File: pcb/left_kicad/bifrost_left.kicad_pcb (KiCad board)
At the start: 2 copper layers, 142.9 x 80.3 mm, 66 parts, among them J1 HRO_TYPE-C-31-M-12, J2 Conn_01x02, J3 Conn_01x06, Q1 AO3401A, Q2 2N7002, Q3 AO3401A, SW1 1.5U, SW10 SW_Push, SW11 SW_Push, SW12 1.25U, SW13 SW_Push, SW14 SW_Push, SW15 SW_Push, SW16 SW_Push, SW17 SW_Push, SW18 SW_Push, SW19 SW_Push, SW2 1.75U, SW20 SW_Push, SW21 SW_Push, SW3 SW_Push, SW4 1.25U, SW5 SW_Push, SW6 SW_Push, SW7 SW_Push, SW8 1.25U, SW9 SW_Push, T1 SW_Push_Shielded, U1 MDBT50Q-1MV2, U2 TP4057, U3 SRV05-4, X1 32.768kHz

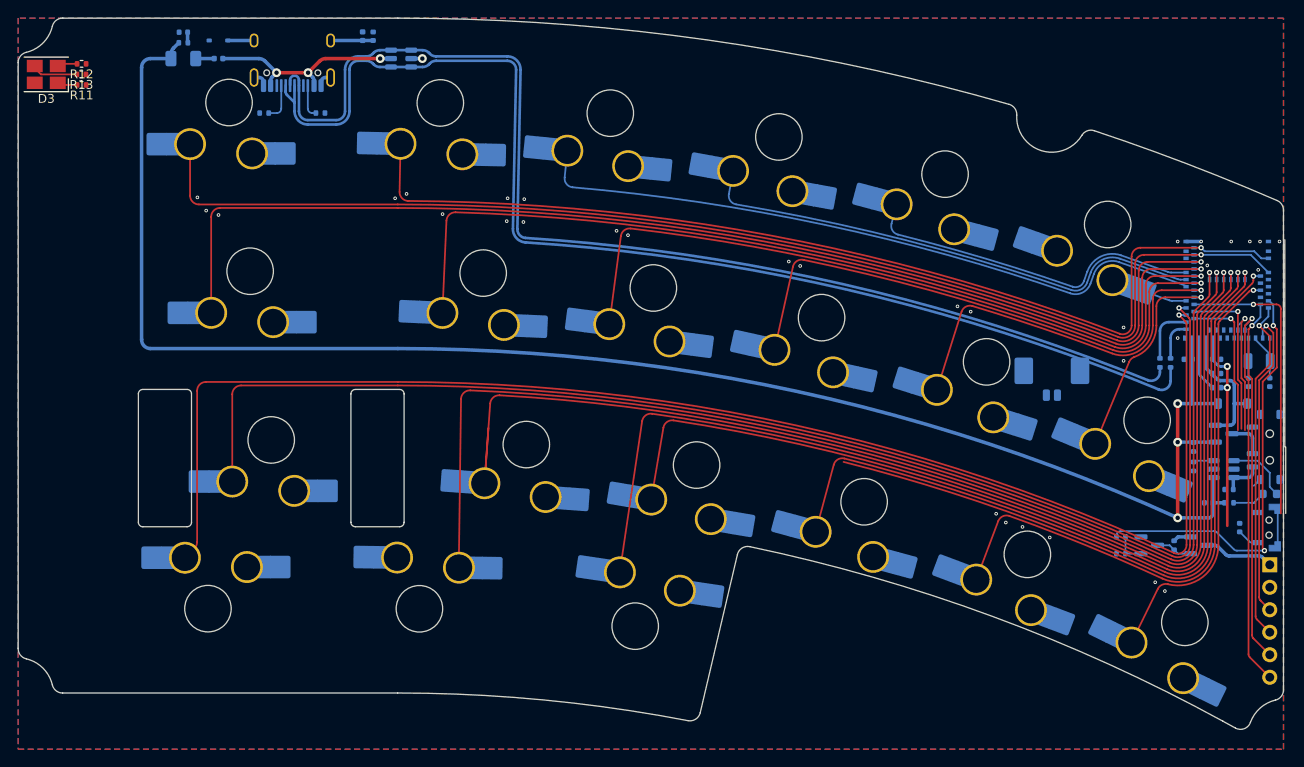
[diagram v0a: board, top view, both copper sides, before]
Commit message: Update KiCad keyboard designs
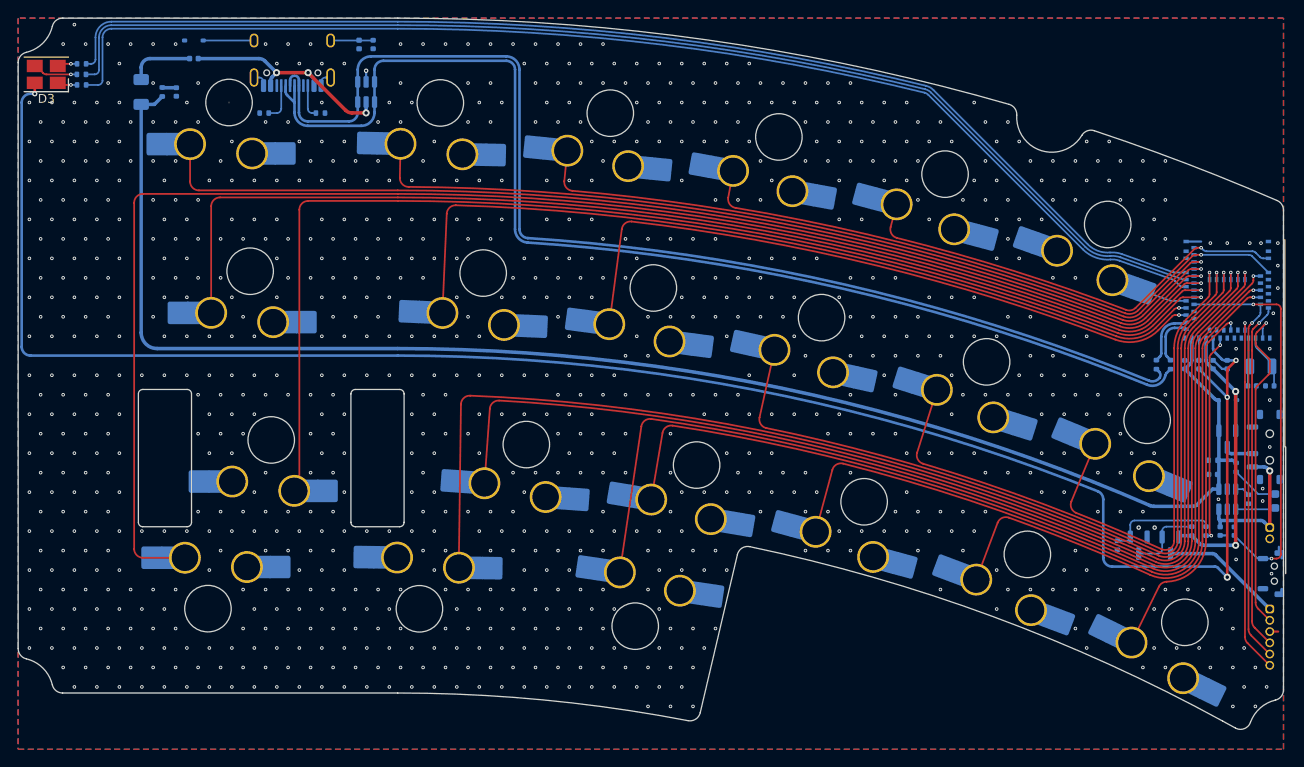
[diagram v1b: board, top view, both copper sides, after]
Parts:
- D1: value 1N5819W -> 1N5819WS; footprint Diode_SMD:D_SOD-123 -> Diode_SMD:D_SOD-323
- J2: footprint Connector_Molex:Molex_PicoBlade_53398-0271_1x02-1MP_P1.25mm_Vertical -> Connector_PinHeader_1.27mm:PinHeader_1x02_P1.27mm_Vertical
- J3: footprint Connector_PinHeader_2.54mm:PinHeader_1x06_P2.54mm_Vertical -> Connector_PinHeader_1.27mm:PinHeader_1x06_P1.27mm_Vertical
- R11, R12, R13: moved to B.Cu
- T1: value SW_Push_Shielded -> TS24CA
- moved J2 29.5 mm to (122.3, 48.0), turned to 180 degrees
- moved R9 9.62 mm to (115.1, 48.4), turned to 90 degrees
- moved R7 7.22 mm to (119.9, 44.8)
- moved C10 6.79 mm to (-1.19, -1.19), turned to -90 degrees
- moved F1 6.07 mm to (-5.16, -1.19), turned to -90 degrees
- moved R8 6.05 mm to (-2.78, -1.19), turned to -90 degrees
- moved U3 5.46 mm to (20.2, -1.19), turned to -90 degrees
- moved T1 5.23 mm to (122.5, 53.2)
- moved J3 5.00 mm to (122.3, 57.2)
- moved C9 4.81 mm to (116.7, 48.4), turned to -90 degrees
- moved R3 4.08 mm to (118.5, 41.2), turned to -90 degrees
- moved U2 3.42 mm to (117.5, 44.8), turned to 90 degrees
- moved L1 3.28 mm to (114.3, 29.6), turned to 90 degrees
- moved C7 3.24 mm to (115.9, 42.0)
- moved Q3 3.20 mm to (111.1, 50.0), turned to -90 degrees
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- renumbered LED1 to CHG1
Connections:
- J2 pad 1: GND -> +BATT
- J2 pad 2: +BATT -> GND
- J3 pad 2: GND -> RGB
- J3 pad 3: RGB -> GND
- SW3 pad 1: PIN_3 -> GND
- SW3 pad 2: GND -> PIN_3
- T1 pad 1: /nRESET -> GND
- T1 pad 2: GND -> /nRESET
- U1 pad 11: unconnected-(U1-P0.02-Pad11) -> PIN_21
- U1 pad 12: RGB_EN -> unconnected-(U1-P0.31-Pad12)
- U1 pad 21: LED_RED -> unconnected-(U1-P0.05-Pad21)
- U1 pad 23: unconnected-(U1-P0.07-Pad23) -> PIN_22
- U1 pad 26: unconnected-(U1-P1.09-Pad26) -> RGB_EN
- U1 pad 3: PIN_5 -> PIN_16
- U1 pad 36: LED_GREEN -> unconnected-(U1-P0.14-Pad36)
- U1 pad 37: PIN_4 -> PIN_10
- U1 pad 38: LED_BLUE -> unconnected-(U1-P0.16-Pad38)
- U1 pad 39: PIN_3 -> PIN_6
- U1 pad 4: PIN_1 -> PIN_13
- U1 pad 42: PIN_20 -> PIN_3
- U1 pad 43: PIN_17 -> PIN_2
- U1 pad 44: PIN_9 -> LED_RED
- U1 pad 45: PIN_14 -> PIN_4
- U1 pad 46: PIN_13 -> LED_BLUE
- U1 pad 47: PIN_10 -> PIN_1
- U1 pad 48: PIN_16 -> LED_GREEN
- U1 pad 49: PIN_6 -> PIN_5
- U1 pad 5: PIN_21 -> PIN_15
- U1 pad 50: PIN_2 -> PIN_9
- U1 pad 56: PIN_18 -> PIN_12
- U1 pad 57: PIN_15 -> PIN_11
- U1 pad 58: PIN_12 -> PIN_8
- U1 pad 59: PIN_11 -> PIN_14
- U1 pad 60: PIN_8 -> PIN_17
- U1 pad 61: PIN_7 -> PIN_20
- U1 pad 9: PIN_22 -> PIN_18
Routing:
- net +3V3: track 23.2 -> 211.2 mm, vias 2 -> 4
- net LED_RED: track 14.6 -> 138.6 mm, vias 1 -> 0
- net LED_GREEN: track 17.1 -> 136.4 mm, vias 1 -> 0
- net LED_BLUE: track 18.4 -> 137.5 mm, vias 1 -> 0
- net PIN_7: track 117.5 -> 0.00 mm, vias 1 -> 0
- net PIN_20: track 23.9 -> 53.5 mm
- net PIN_17: track 43.5 -> 73.0 mm
- net PIN_14: track 64.1 -> 92.4 mm
- net RGB_EN: track 47.4 -> 23.4 mm
- net +5V: track 195.8 -> 175.6 mm, vias 3 -> 0
- net +VSW: track 17.6 -> 36.2 mm, vias 0 -> 2
- net PIN_15: track 87.6 -> 105.7 mm
- net PIN_5: track 115.1 -> 99.7 mm
- net PIN_1: track 138.8 -> 123.5 mm
- net +BATT: track 4.45 -> 16.5 mm, vias 0 -> 1
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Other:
- outline, holes or cut-outs redrawn

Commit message: Update PCB designs
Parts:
- SW10, SW11, SW13, SW14, SW15, SW16, SW17, SW18, SW19, SW20, SW21, SW5, SW6, SW7, SW9: value SW_Push -> 1U
- SW3: value SW_Push -> 2U

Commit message: Update PCB and case designs
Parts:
- moved C3 111.7 mm to (207.1, 89.1)
- moved C9 111.7 mm to (211.1, 107.9)
- moved L2 111.7 mm to (113.9, 53.0)
- moved Q3 111.7 mm to (205.5, 109.5)
- moved R1 111.7 mm to (205.5, 89.1)
- moved R10 111.7 mm to (199.5, 109.5)
- moved R6 111.7 mm to (109.5, 60.7)
- moved R8 111.7 mm to (91.7, 58.3)
- moved R9 111.7 mm to (209.5, 107.9)
- moved SW11 111.7 mm to (152.0, 100.5)
- moved SW13 111.7 mm to (161.3, 63.4)
- moved SW14 111.7 mm to (166.1, 83.8)
- moved SW15 111.7 mm to (170.9, 104.6)
- moved SW16 111.7 mm to (180.1, 67.6)
- moved C1 111.7 mm to (210.3, 89.1)
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
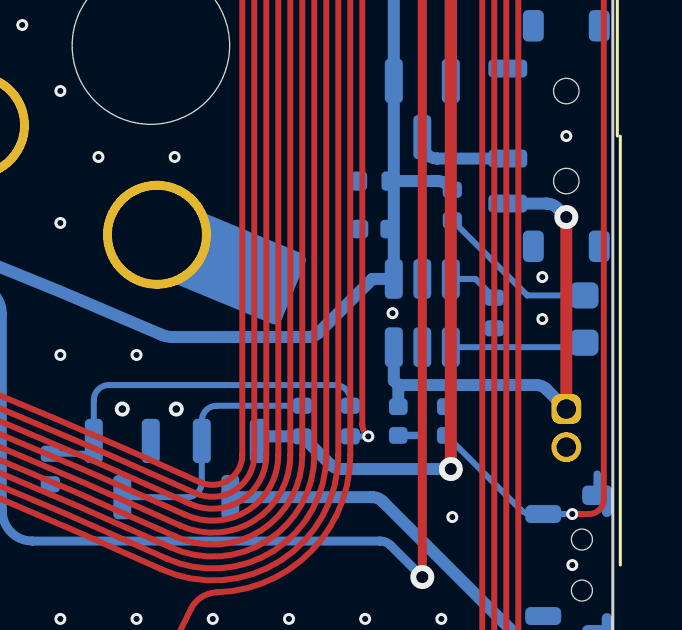
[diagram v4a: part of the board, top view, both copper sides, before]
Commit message: Update PCB fabrication outputs and switch knob
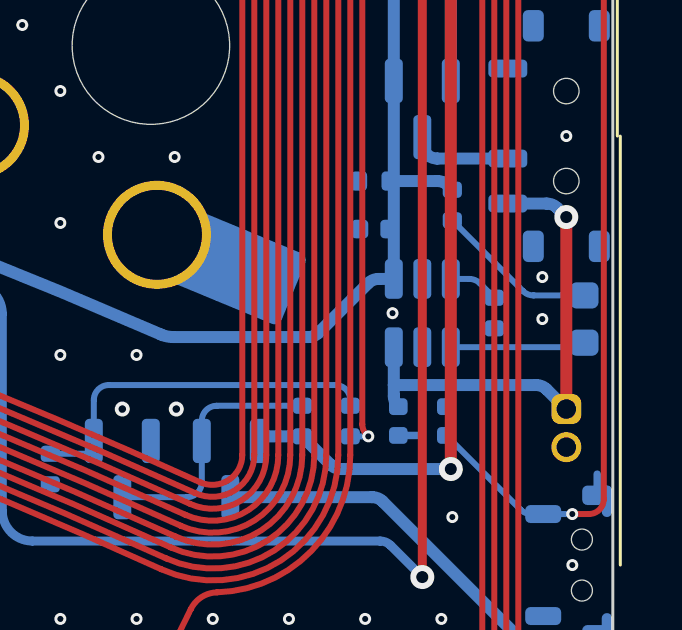
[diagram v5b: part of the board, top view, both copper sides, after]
